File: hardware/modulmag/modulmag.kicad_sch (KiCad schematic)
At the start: 48 parts, among them J1 DEBUG, J2 BUS_IN, J3 BUS_OUT, U1 P78E05-1000, U2 ISO1042BDWV, U3 ESD2CAN24-Q1, U5 NCP1117ST33T3G, U6 STM32F303RET6, Y1 8MHz

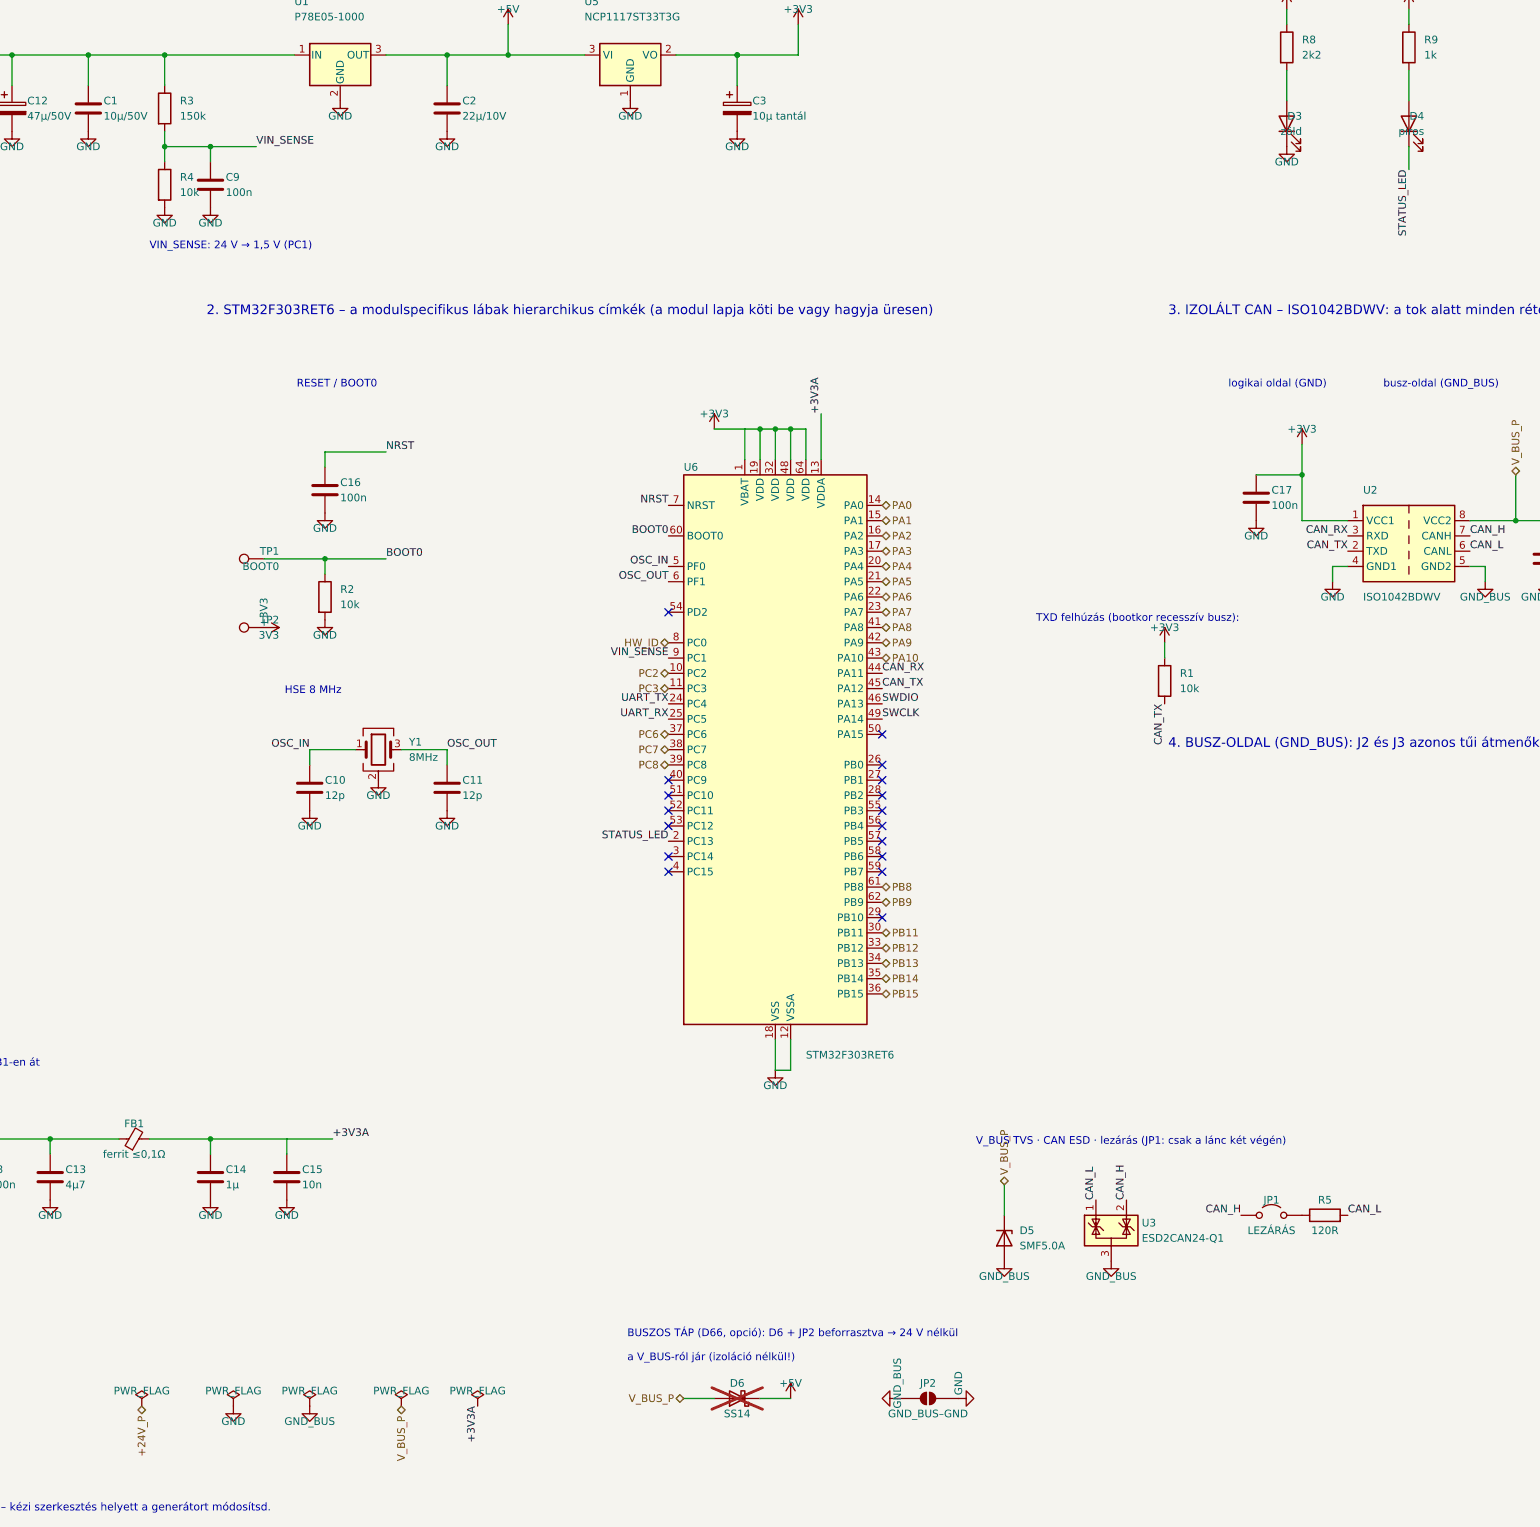
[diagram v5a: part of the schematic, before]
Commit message: Hardver: kapcsolási rajzok olvashatósága (KiCad MCP vizuális ellenőrzés alapján), output/ gitignore
Co-Authored-By: Claude Opus 5.5 <noreply@anthropic.com>
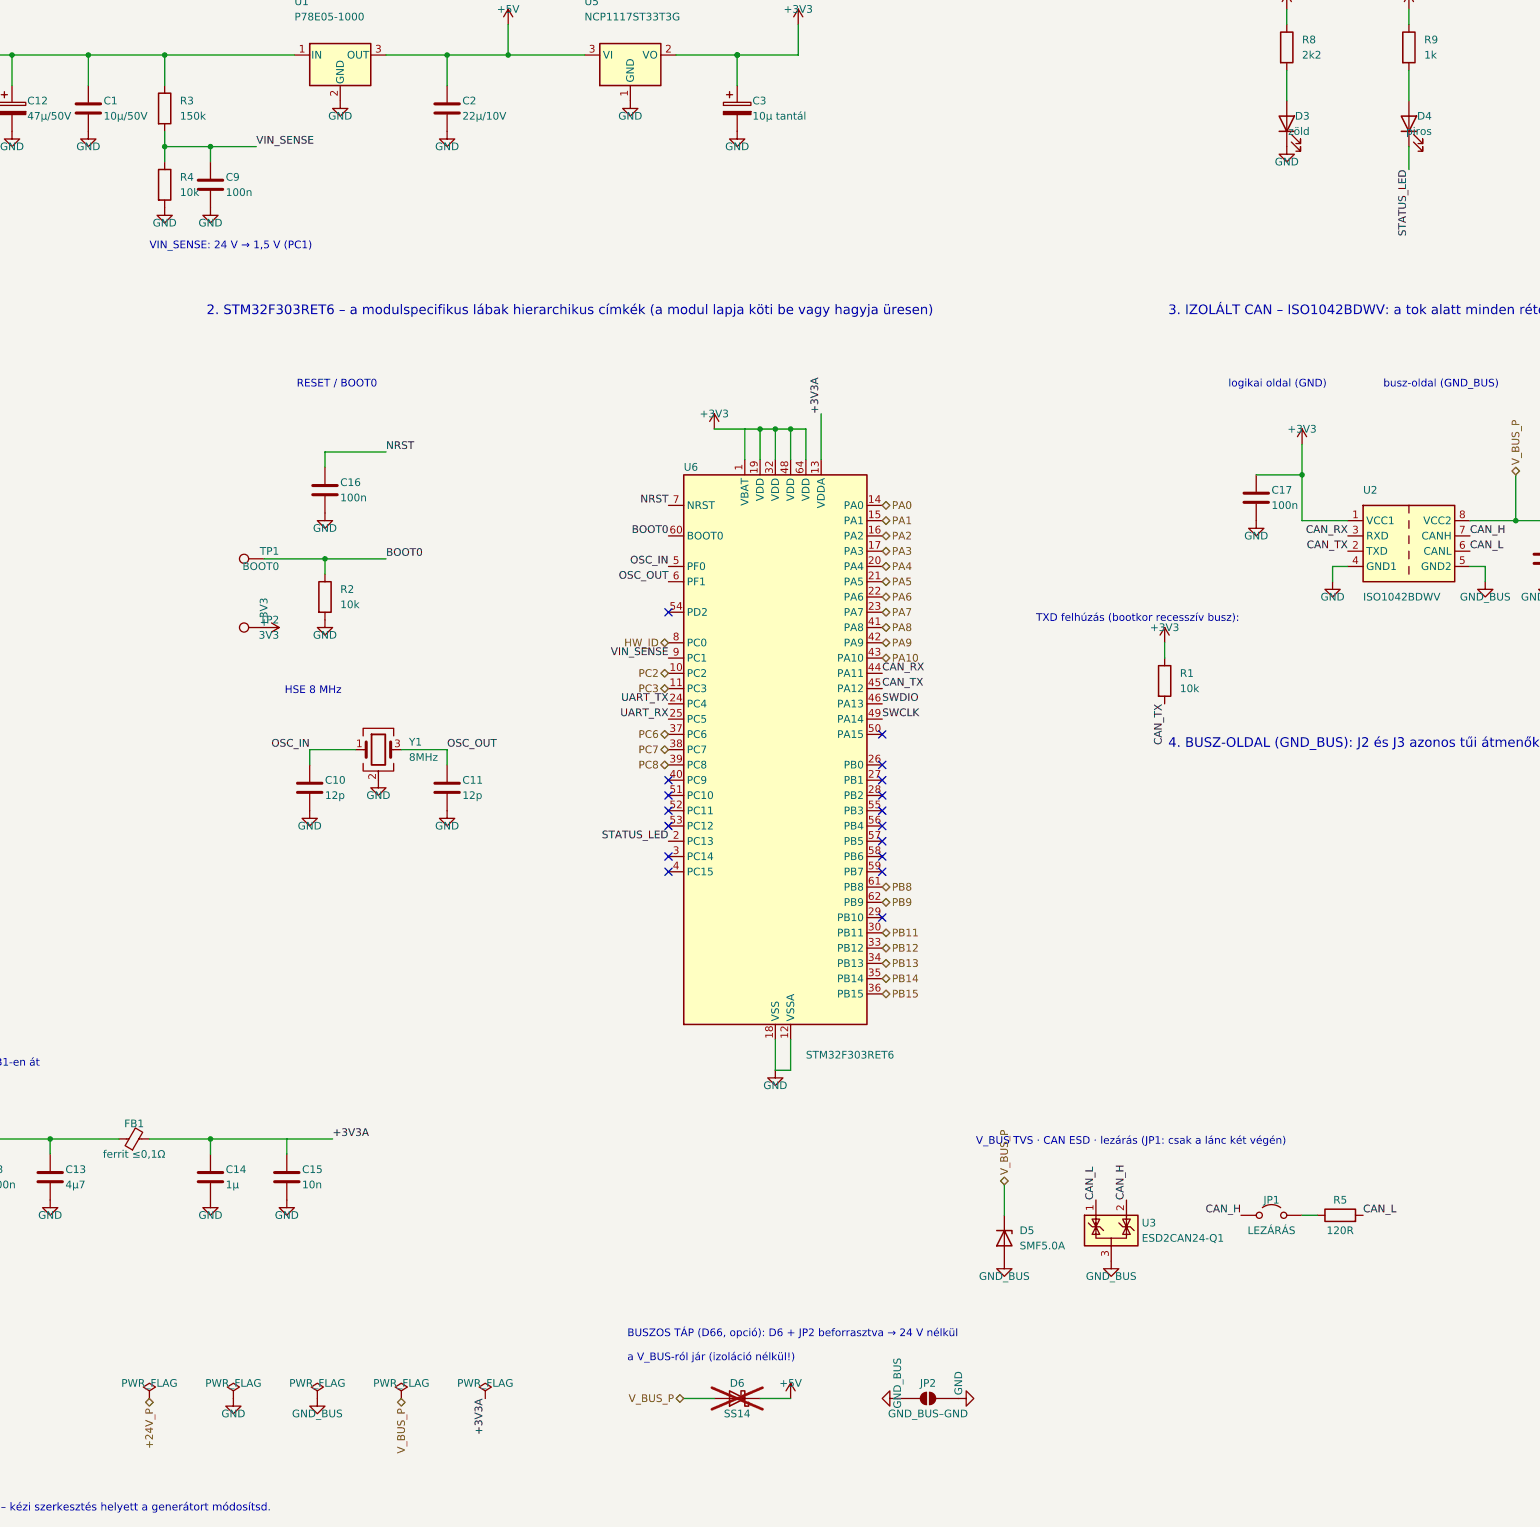
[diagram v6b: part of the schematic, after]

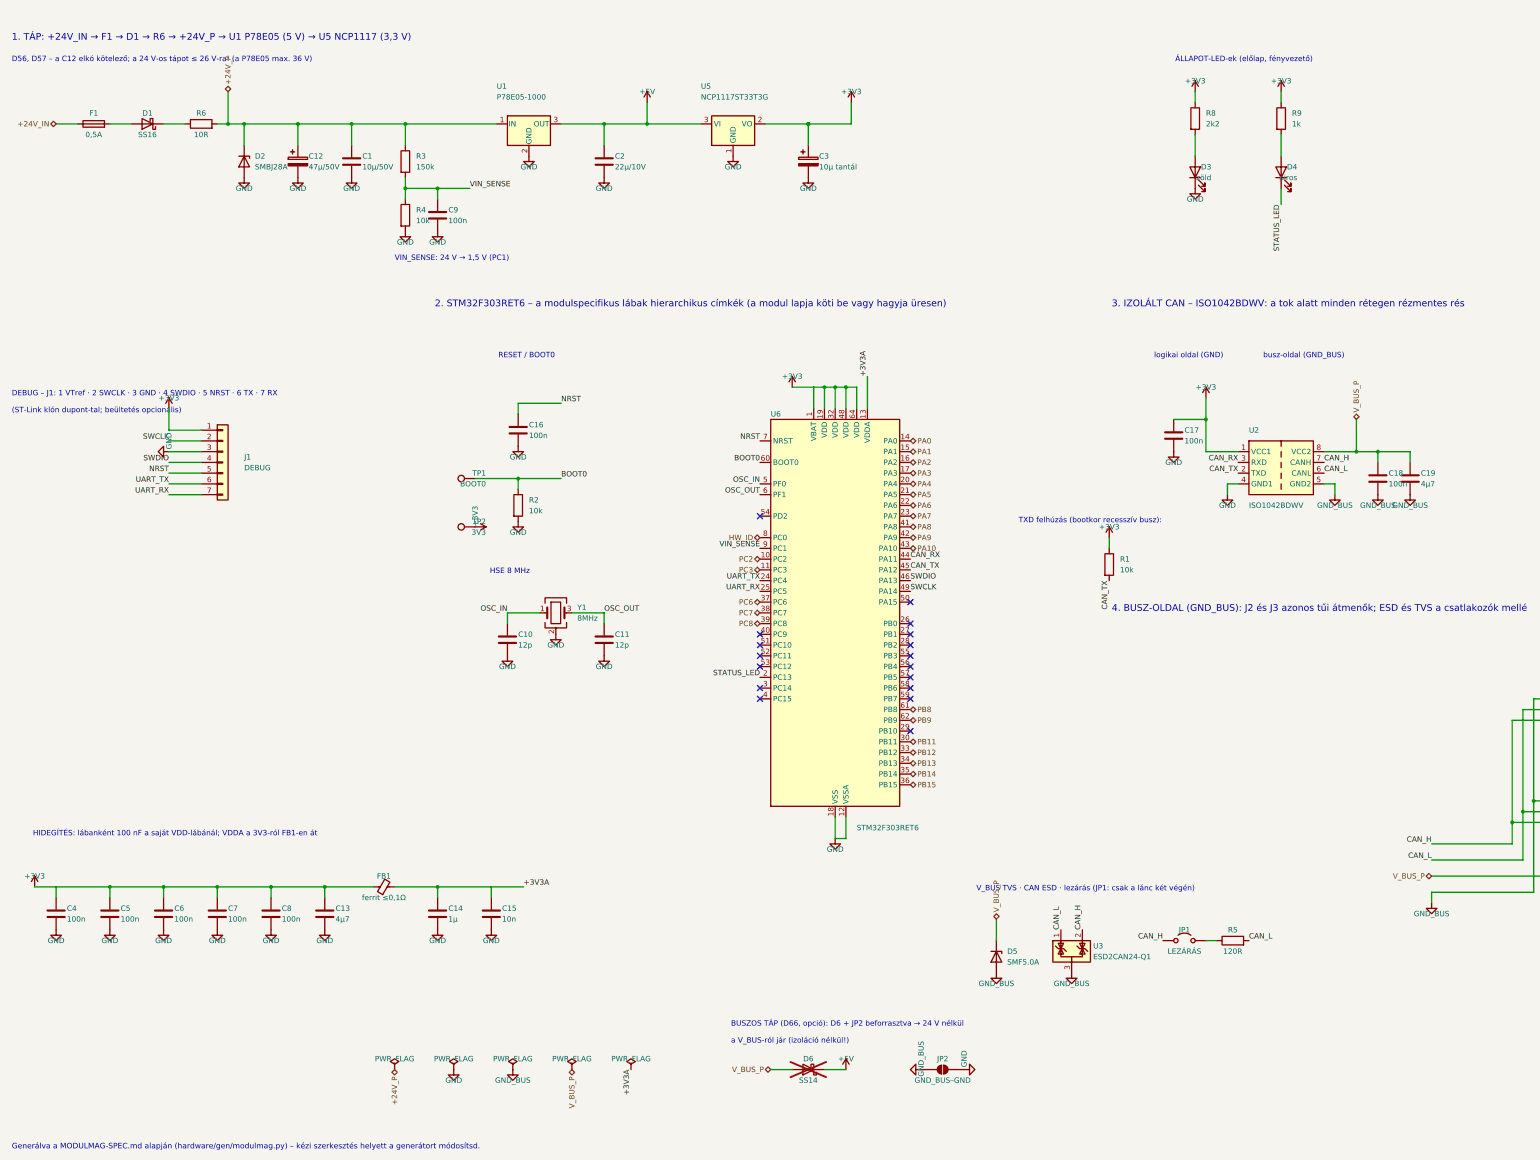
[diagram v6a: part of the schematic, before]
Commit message: Hardver: átnézés (C320 javítva), LoRa-előkészítés (D68), bővítők (D69), R6/R7 = 0 Ω (D70)
- bemeneti modul: a HDC3020 hidegítője C330 lett (a C320 kétszer szerepelt);
  a generátor mostantól hibát dob duplikált jelölésre
- vezérlő: E22-900M22S LoRa + u.FL + 74LVC1G04, minden DNP; J8 bővítő (GPIO5),
  7 mérőpont; spec szerinti DNP-k (USB C, 1 MΩ, PMODE, CAN-fojtó + áthidalók);
  saját footprint az LMR36015-höz (RNX) és az E22-höz
- modulmag: HW_REV osztó (PB0), DNP J4 2 × 5 bővítő; relé: DNP SCT-013 → PA0
- mind az öt lap vizuálisan rendbe téve; R6/R7 = 0 Ω
- specek és döntésnapló frissítve (D68–D70)

Co-Authored-By: Claude Opus 5.5 <noreply@anthropic.com>
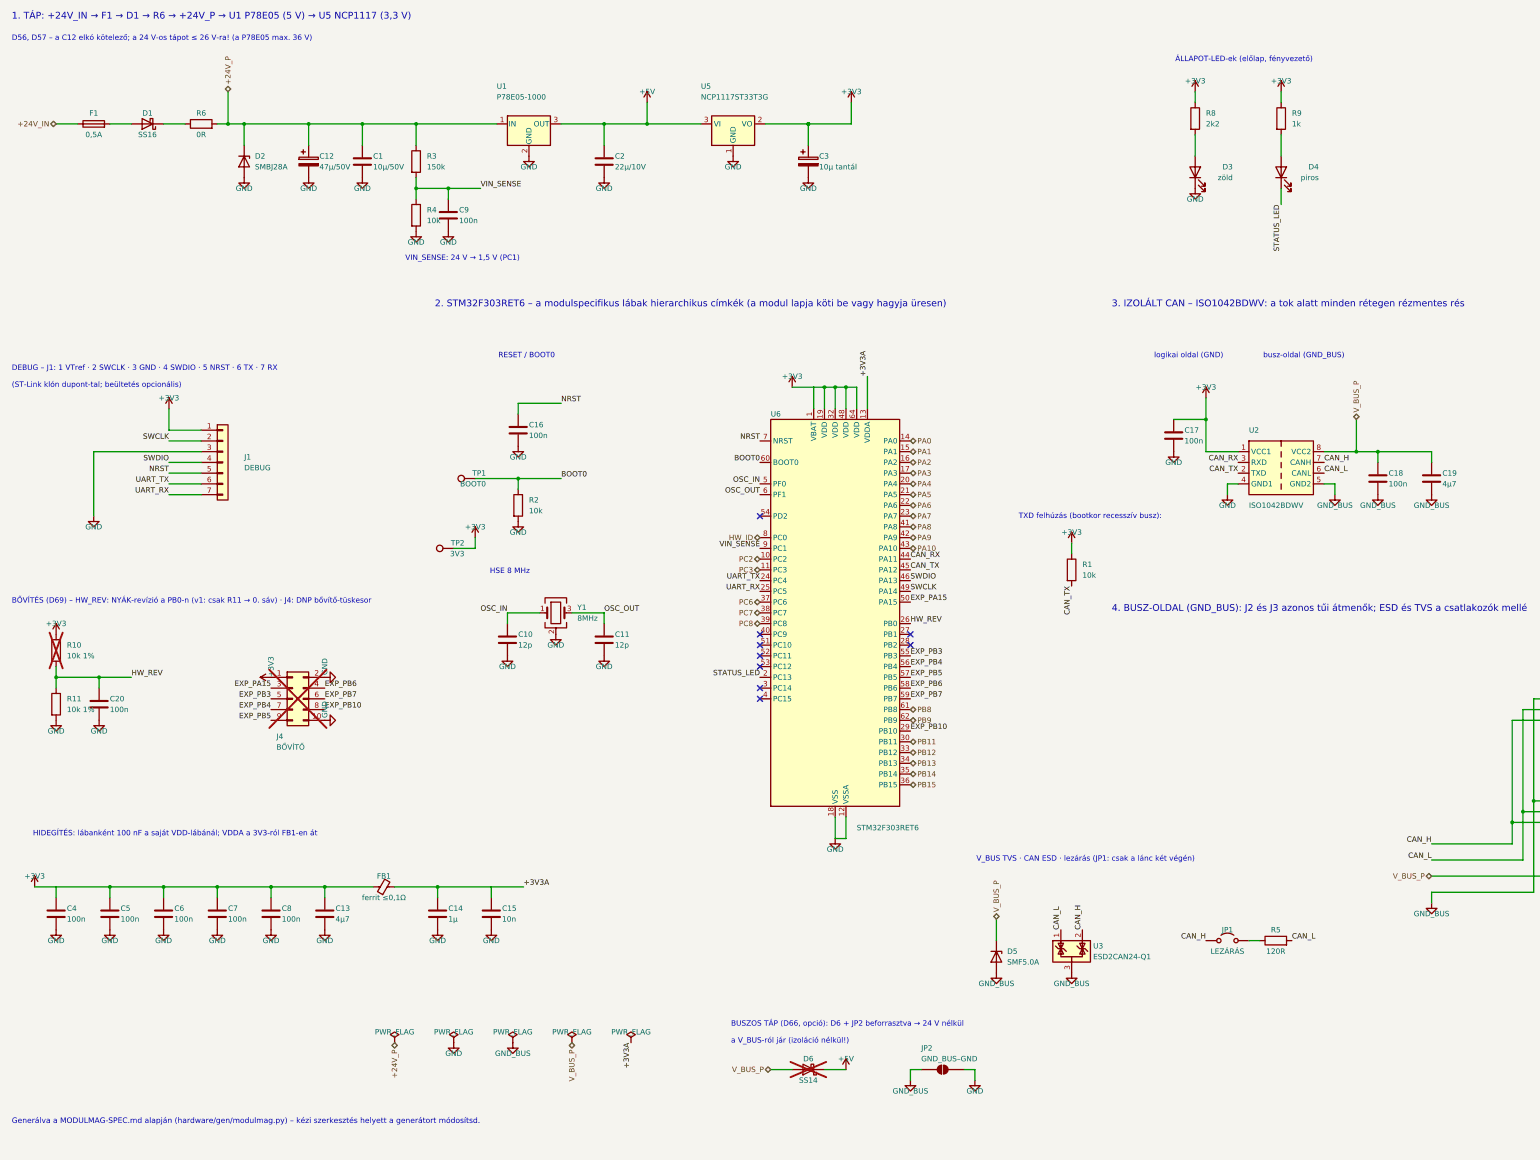
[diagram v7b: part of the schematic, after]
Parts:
- added C20: 100n, Capacitor_SMD:C_0603_1608Metric, symbol Device:C
- added J4: BŐVÍTŐ, Connector_PinHeader_2.54mm:PinHeader_2x05_P2.54mm_Vertical, symbol Connector_Generic:Conn_02x05_Odd_Even
- added R10, R11: 10k 1%, Resistor_SMD:R_0603_1608Metric, symbol Device:R
- R6: value 10R -> 0R; Megjegyzés impulzusbíró (pl. ERJ-P08); 0 Ω-mal áthidalható (D57) -> D70: 0 Ω; a footprint marad – szükség esetén 10 Ω impulzusb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
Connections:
- net +3V3: now also J4.1 (Pin_1), R10.1
- net GND: now also C20.2, J4.10 (Pin_10), J4.2 (Pin_2), R11.2
- net HW_REV: now reaches U6.26 (PB0)
- net HW_REV: now also C20.1, R10.2, R11.1
- net EXP_PB10: now reaches U6.29 (PB10)
- net EXP_PB10: now also J4.8 (Pin_8)
- net EXP_PA15: now reaches U6.50 (PA15)
- net EXP_PA15: now also J4.3 (Pin_3)
- net EXP_PB3: now reaches U6.55 (PB3)
- net EXP_PB3: now also J4.5 (Pin_5)
- net EXP_PB4: now reaches U6.56 (PB4)
- net EXP_PB4: now also J4.7 (Pin_7)
- net EXP_PB5: now reaches U6.57 (PB5)
- net EXP_PB5: now also J4.9 (Pin_9)
- net EXP_PB6: now reaches U6.58 (PB6)
- net EXP_PB6: now also J4.4 (Pin_4)
- net EXP_PB7: now reaches U6.59 (PB7)
- net EXP_PB7: now also J4.6 (Pin_6)
- no-connect marks 17 -> 9
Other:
- note added: "BŐVÍTÉS (D69) – HW_REV: NYÁK-revízió a PB0-n (v1: csak R11 → 0. sáv) · J4: DNP bővítő-tüskesor"
- title: Modulmag – STM32F303RET6 + izolált CAN + 24 V → 5 V → 3,3 V -> Modulmag – STM32F303RET6, izolált CAN, 24 → 5 → 3,3 V
